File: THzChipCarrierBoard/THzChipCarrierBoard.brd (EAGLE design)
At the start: 34.3 x 26.7 mm, 8 parts

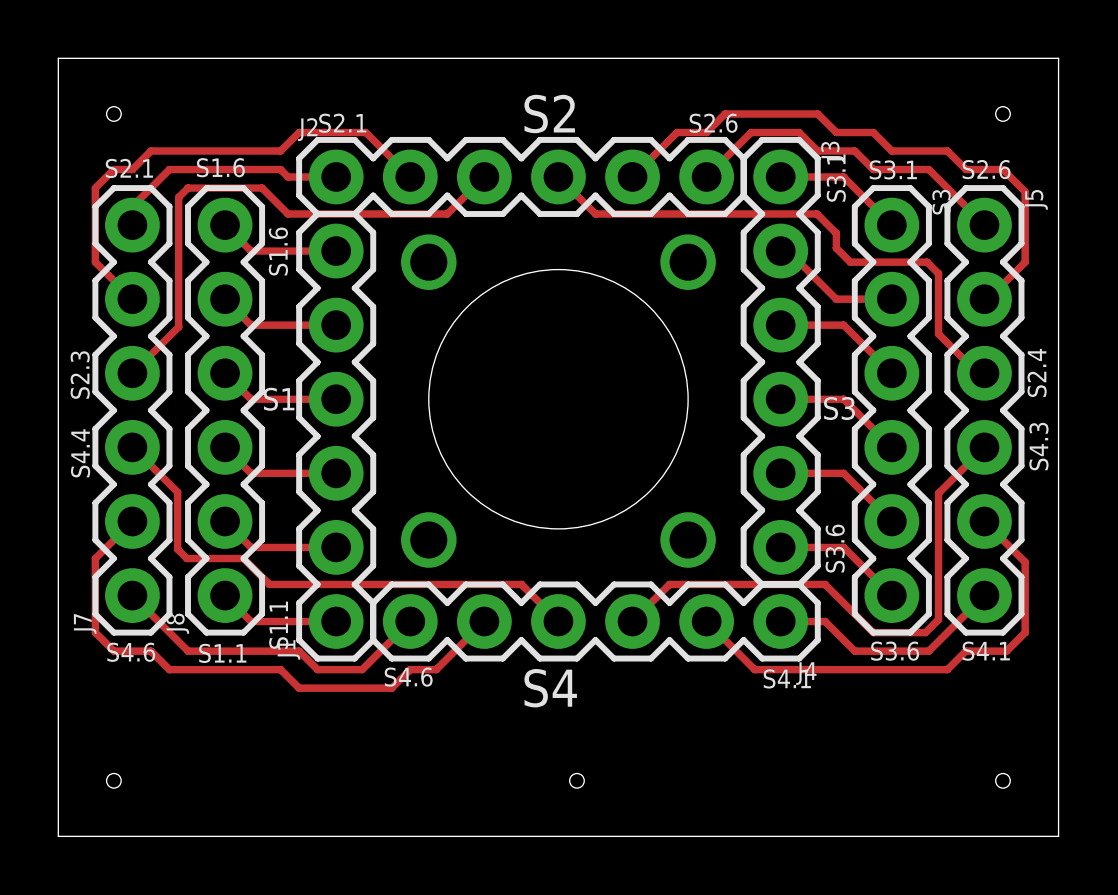
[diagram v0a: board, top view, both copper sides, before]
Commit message: Updated ChipCarrier board design, added copper plate backing, soldermasks and what not
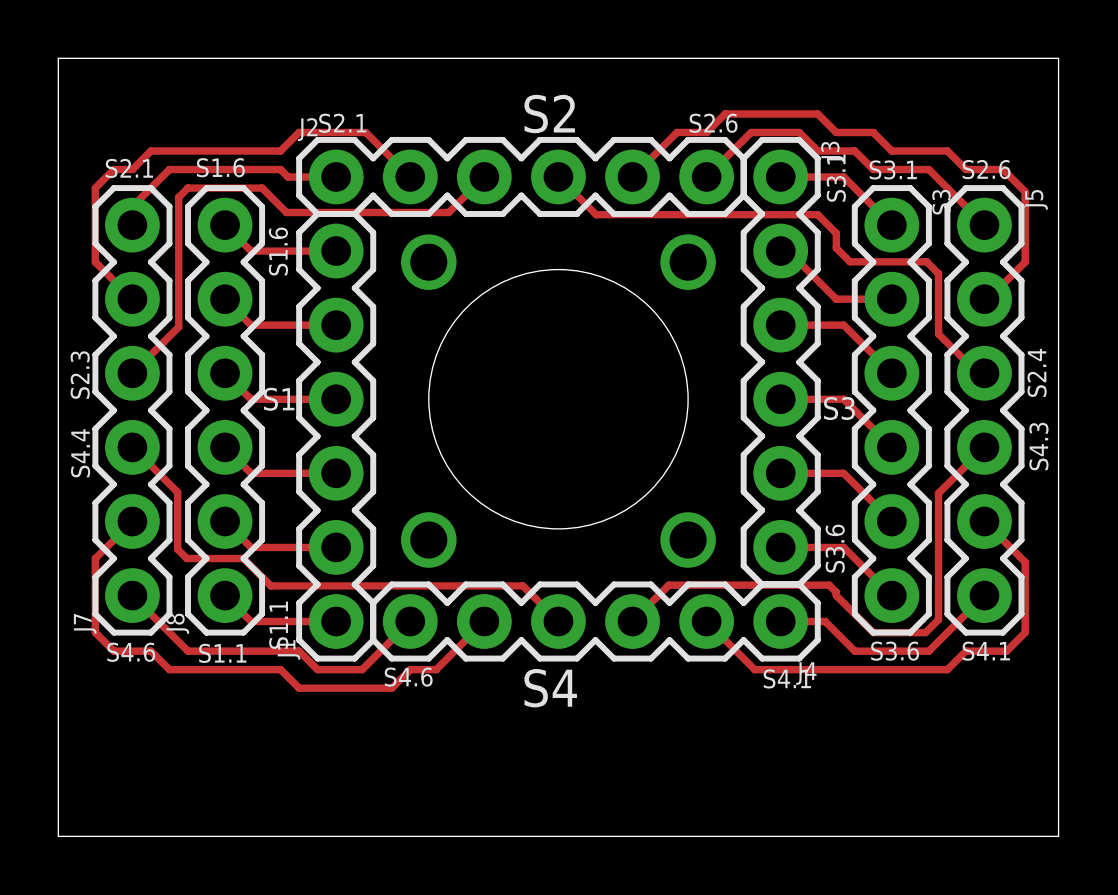
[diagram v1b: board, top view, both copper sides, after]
